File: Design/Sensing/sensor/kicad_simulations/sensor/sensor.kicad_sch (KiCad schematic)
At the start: 44 parts, among them J1 Conn_02x14_Counter_Clockwise, J10 Conn_01x02_Pin, J11 Conn_01x01_Pin, J12 Conn_01x02_Pin, J13 Conn_01x02_Pin, J14 Conn_01x02_Pin, J15 Conn_01x02_Pin, J16 Conn_01x01_Pin, J17 Conn_01x02_Pin, J18 Conn_01x01_Pin, J3 Conn_01x02_Pin, J4 Conn_01x02_Pin, J5 Conn_01x02_Pin, J6 Conn_01x01_Pin, J7 Conn_01x02_Pin, J8 Conn_01x02_Pin, J9 Conn_01x02_Pin, Q1 2N3904, Q2 2N3904, Q3 2N3904, U1 TSSP58038, U2 TSSP58038, U3 TSSP58038, U4 BUF602xD, U5 BUF602xD, U6 BUF602xD

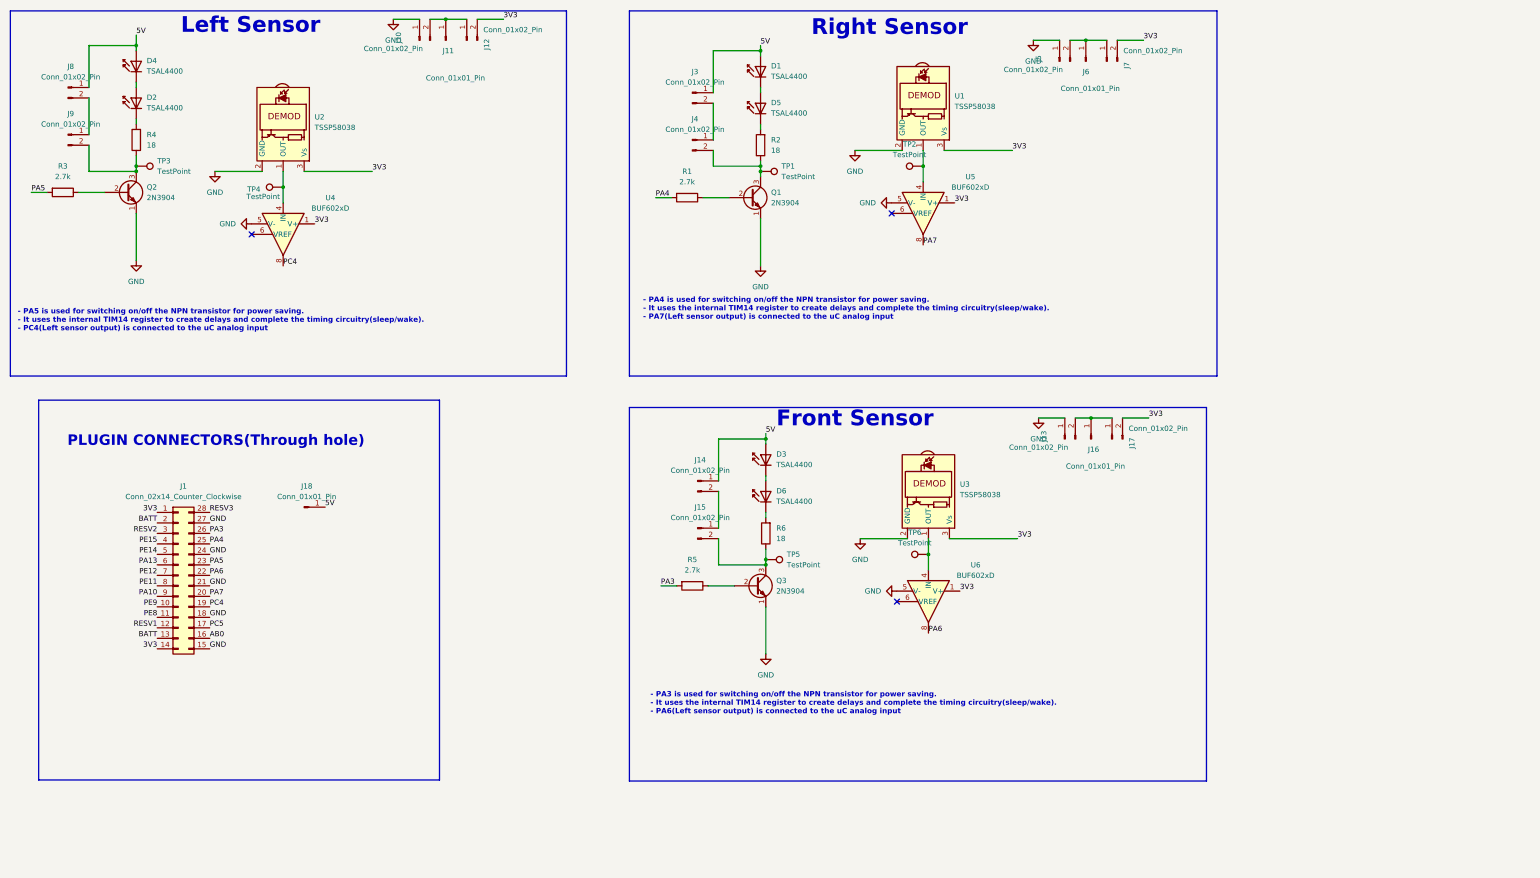
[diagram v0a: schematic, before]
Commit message: PCB placement done, now need to root/make track connections
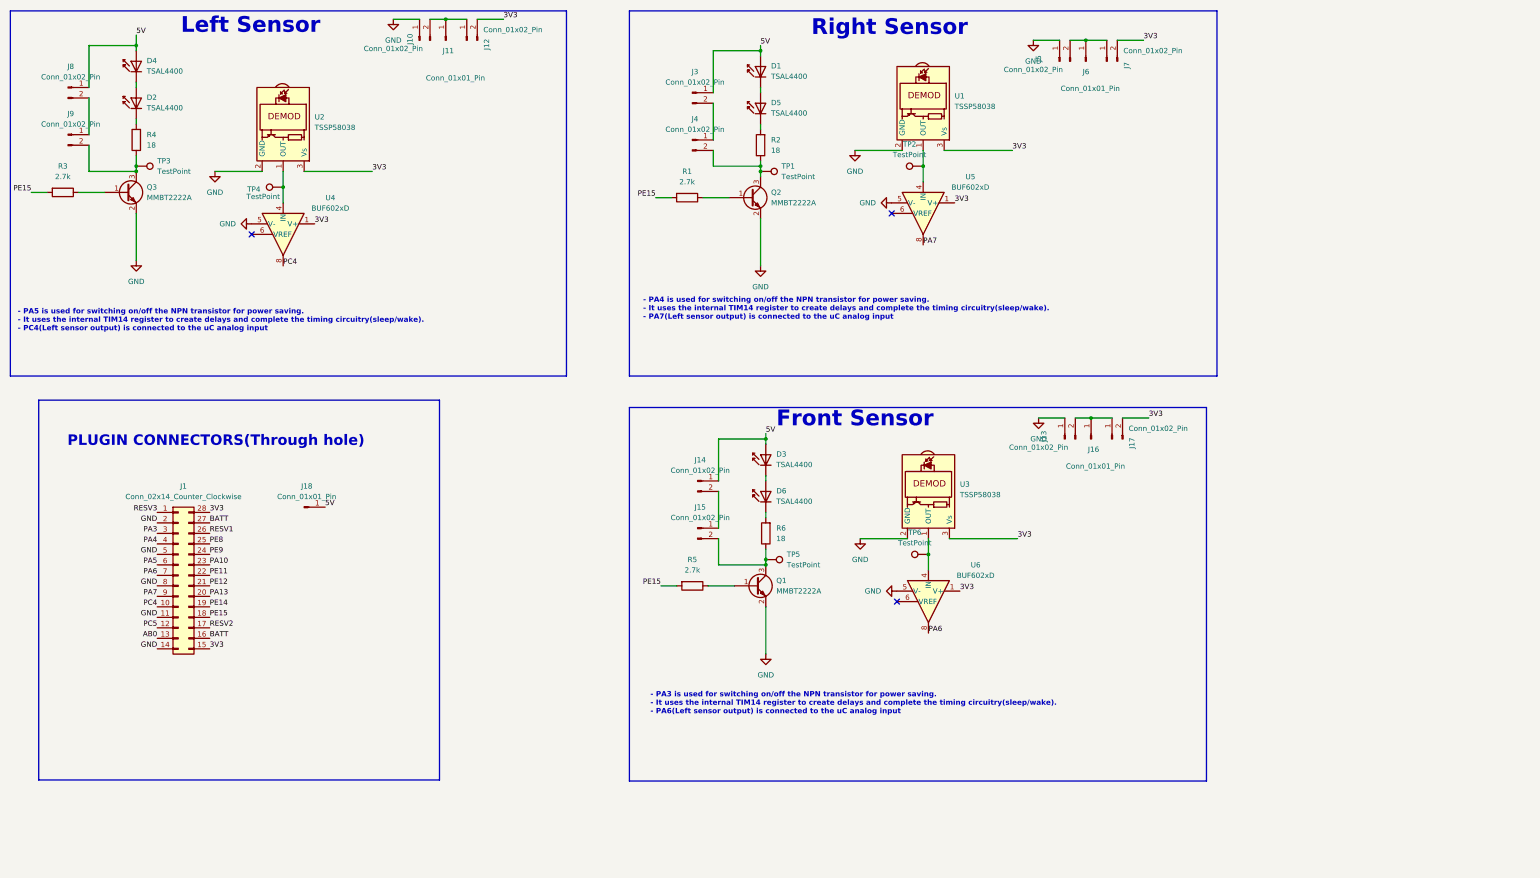
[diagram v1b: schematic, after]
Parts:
- removed Q1, Q2, Q3: 2N3904, Package_TO_SOT_THT:TO-92_Inline, symbol Transistor_BJT:2N3904
- added Q1, Q2, Q3: MMBT2222A, Package_TO_SOT_SMD:SOT-23, symbol Transistor_BJT:MMBT2222A
- D1, D2, D3, D4, D5, D6: footprint LED_THT:LED_D3.0mm_IRBlack -> LED_THT:LED_D3.0mm_Horizontal_O1.27mm_Z2.0mm_IRBlack
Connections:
- net 3V3: now also J1.15 (Pin_15), J1.28 (Pin_28); no longer J1.1 (Pin_1), J1.14 (Pin_14)
- net AB0: now also J1.13 (Pin_13); no longer J1.16 (Pin_16)
- net BATT: now also J1.16 (Pin_16), J1.27 (Pin_27); no longer J1.13 (Pin_13), J1.2 (Pin_2)
- net GND: now also J1.11 (Pin_11), J1.14 (Pin_14), J1.2 (Pin_2), J1.5 (Pin_5), J1.8 (Pin_8), Q1.2 (E), Q2.2 (E), Q3.2 (E); no longer J1.15 (Pin_15), J1.18 (Pin_18), J1.21 (Pin_21), J1.24 (Pin_24), J1.27 (Pin_27)
- net PA10: now also J1.23 (Pin_23); no longer J1.9 (Pin_9)
- net PA13: now also J1.20 (Pin_20); no longer J1.6 (Pin_6)
- net PA3: now also J1.3 (Pin_3); no longer J1.26 (Pin_26), R5.2
- net PA4: now also J1.4 (Pin_4); no longer J1.25 (Pin_25), R1.2
- net PA5: now also J1.6 (Pin_6); no longer J1.23 (Pin_23), R3.2
- net PA6: now also J1.7 (Pin_7); no longer J1.22 (Pin_22)
- net PA7: now also J1.9 (Pin_9); no longer J1.20 (Pin_20)
- net PC4: now also J1.10 (Pin_10); no longer J1.19 (Pin_19)
- net PC5: now also J1.12 (Pin_12); no longer J1.17 (Pin_17)
- net PE11: now also J1.22 (Pin_22); no longer J1.8 (Pin_8)
- net PE12: now also J1.21 (Pin_21); no longer J1.7 (Pin_7)
- net PE14: now also J1.19 (Pin_19); no longer J1.5 (Pin_5)
- net PE15: now also J1.18 (Pin_18), R1.2, R3.2, R5.2; no longer J1.4 (Pin_4)
- net PE8: now also J1.25 (Pin_25); no longer J1.11 (Pin_11)
- net PE9: now also J1.24 (Pin_24); no longer J1.10 (Pin_10)
- net RESV1: now also J1.26 (Pin_26); no longer J1.12 (Pin_12)
- net RESV2: now also J1.17 (Pin_17); no longer J1.3 (Pin_3)
- net RESV3: now also J1.1 (Pin_1); no longer J1.28 (Pin_28)
- net at R5.1: now also Q1.1 (B)
- net at J15.2 (Pin_2), R6.1, TP5.1: now also Q1.3 (C)
- net at J9.2 (Pin_2), R4.1, TP3.1: now also Q3.3 (C)
- net at R1.1: now also Q2.1 (B)
- net at J4.2 (Pin_2), R2.1, TP1.1: now also Q2.3 (C)
- net at R3.1: now also Q3.1 (B)

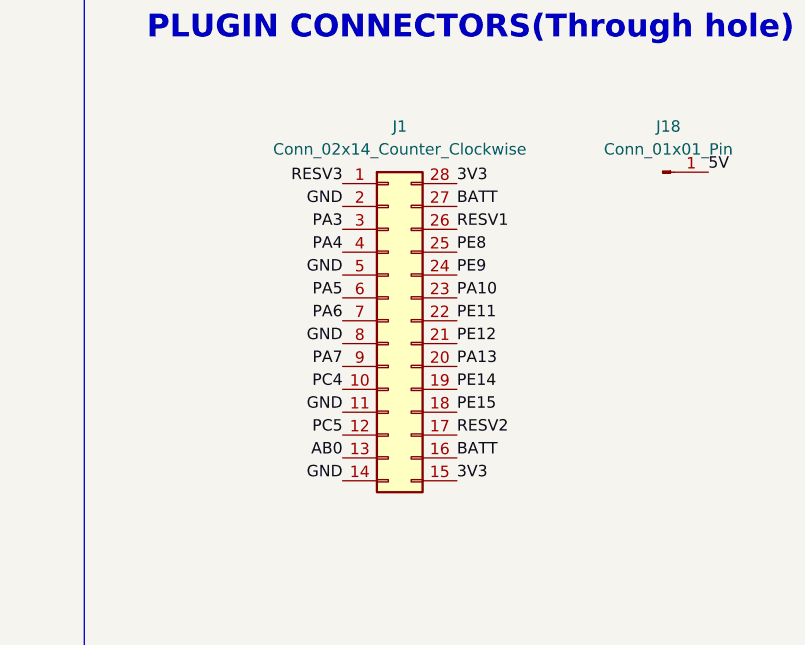
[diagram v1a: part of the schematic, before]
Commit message: PCB track done but still have 23 unrouted
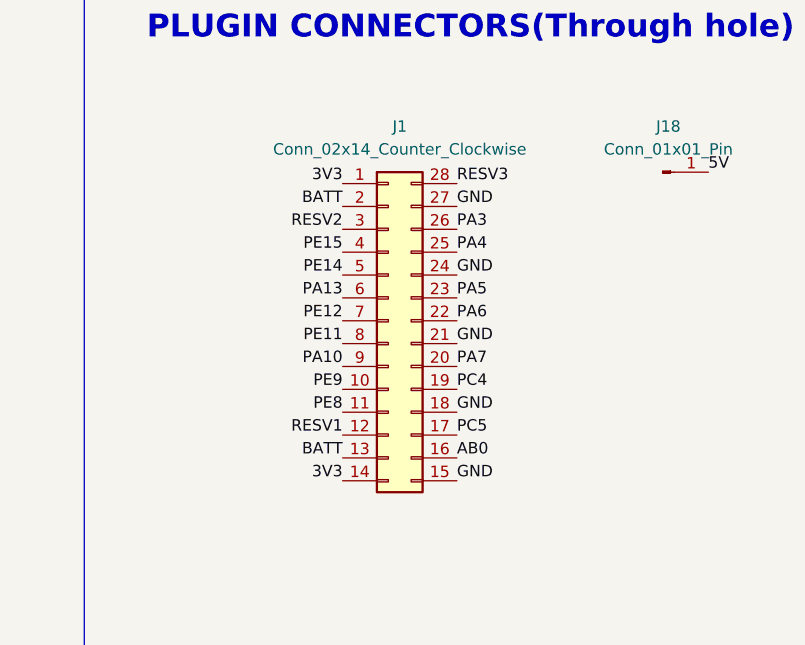
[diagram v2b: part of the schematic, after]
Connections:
- net 3V3: now also J1.1 (Pin_1), J1.14 (Pin_14); no longer J1.15 (Pin_15), J1.28 (Pin_28)
- net AB0: now also J1.16 (Pin_16); no longer J1.13 (Pin_13)
- net BATT: now also J1.13 (Pin_13), J1.2 (Pin_2); no longer J1.16 (Pin_16), J1.27 (Pin_27)
- net GND: now also J1.15 (Pin_15), J1.18 (Pin_18), J1.21 (Pin_21), J1.24 (Pin_24), J1.27 (Pin_27); no longer J1.11 (Pin_11), J1.14 (Pin_14), J1.2 (Pin_2), J1.5 (Pin_5), J1.8 (Pin_8)
- net PA10: now also J1.9 (Pin_9); no longer J1.23 (Pin_23)
- net PA13: now also J1.6 (Pin_6); no longer J1.20 (Pin_20)
- net PA3: now also J1.26 (Pin_26); no longer J1.3 (Pin_3)
- net PA4: now also J1.25 (Pin_25); no longer J1.4 (Pin_4)
- net PA5: now also J1.23 (Pin_23); no longer J1.6 (Pin_6)
- net PA6: now also J1.22 (Pin_22); no longer J1.7 (Pin_7)
- net PA7: now also J1.20 (Pin_20); no longer J1.9 (Pin_9)
- net PC4: now also J1.19 (Pin_19); no longer J1.10 (Pin_10)
- net PC5: now also J1.17 (Pin_17); no longer J1.12 (Pin_12)
- net PE11: now also J1.8 (Pin_8); no longer J1.22 (Pin_22)
- net PE12: now also J1.7 (Pin_7); no longer J1.21 (Pin_21)
- net PE14: now also J1.5 (Pin_5); no longer J1.19 (Pin_19)
- net PE15: now also J1.4 (Pin_4); no longer J1.18 (Pin_18)
- net PE8: now also J1.11 (Pin_11); no longer J1.25 (Pin_25)
- net PE9: now also J1.10 (Pin_10); no longer J1.24 (Pin_24)
- net RESV1: now also J1.12 (Pin_12); no longer J1.26 (Pin_26)
- net RESV2: now also J1.3 (Pin_3); no longer J1.17 (Pin_17)
- net RESV3: now also J1.28 (Pin_28); no longer J1.1 (Pin_1)

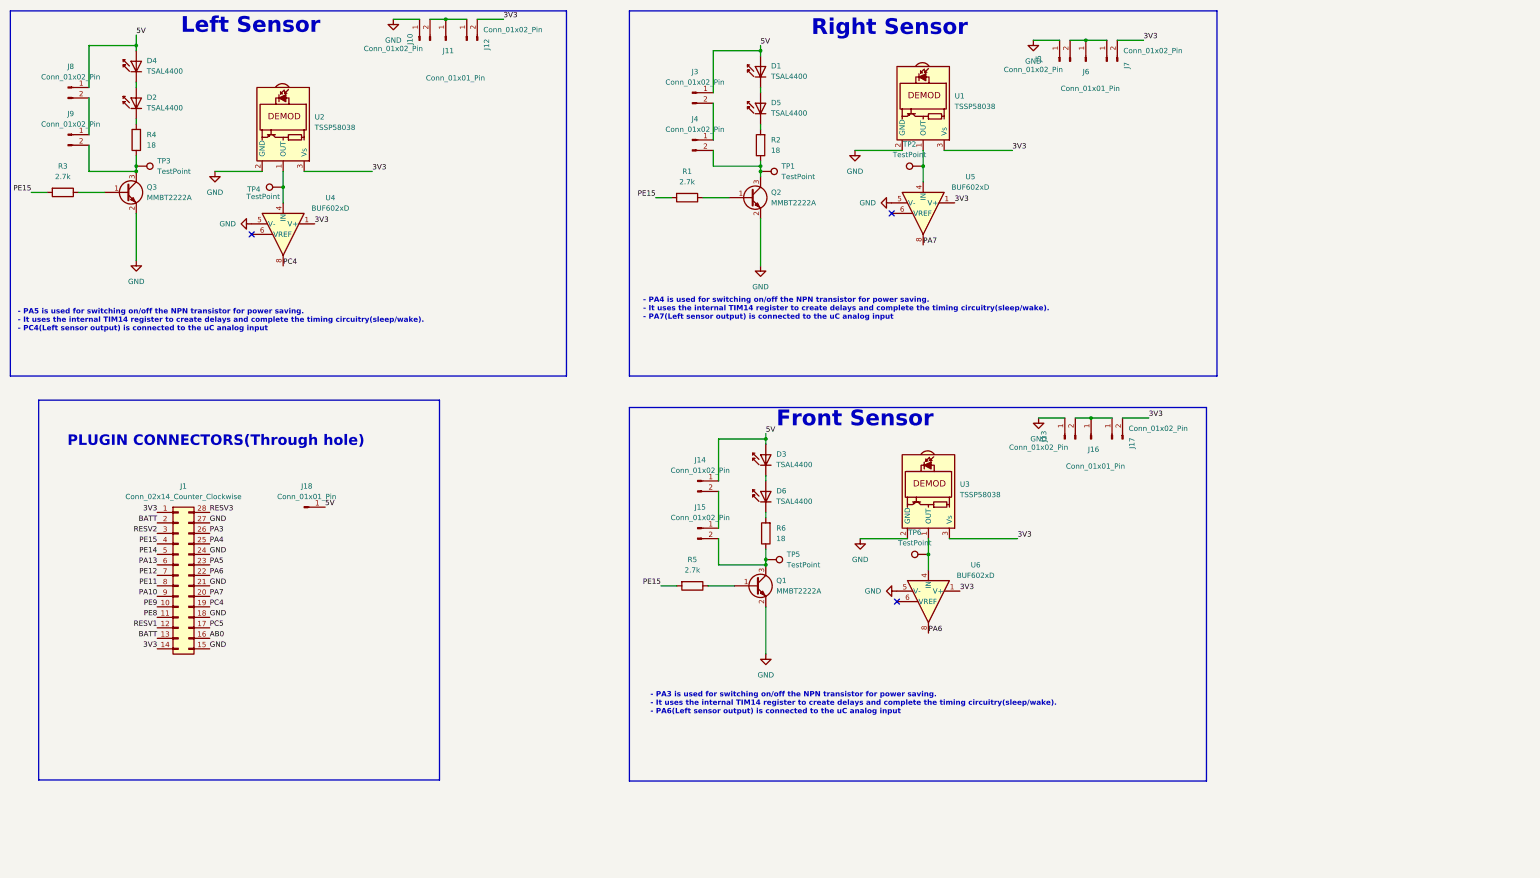
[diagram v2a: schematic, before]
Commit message: Only two unrouted and 3 errors remaining
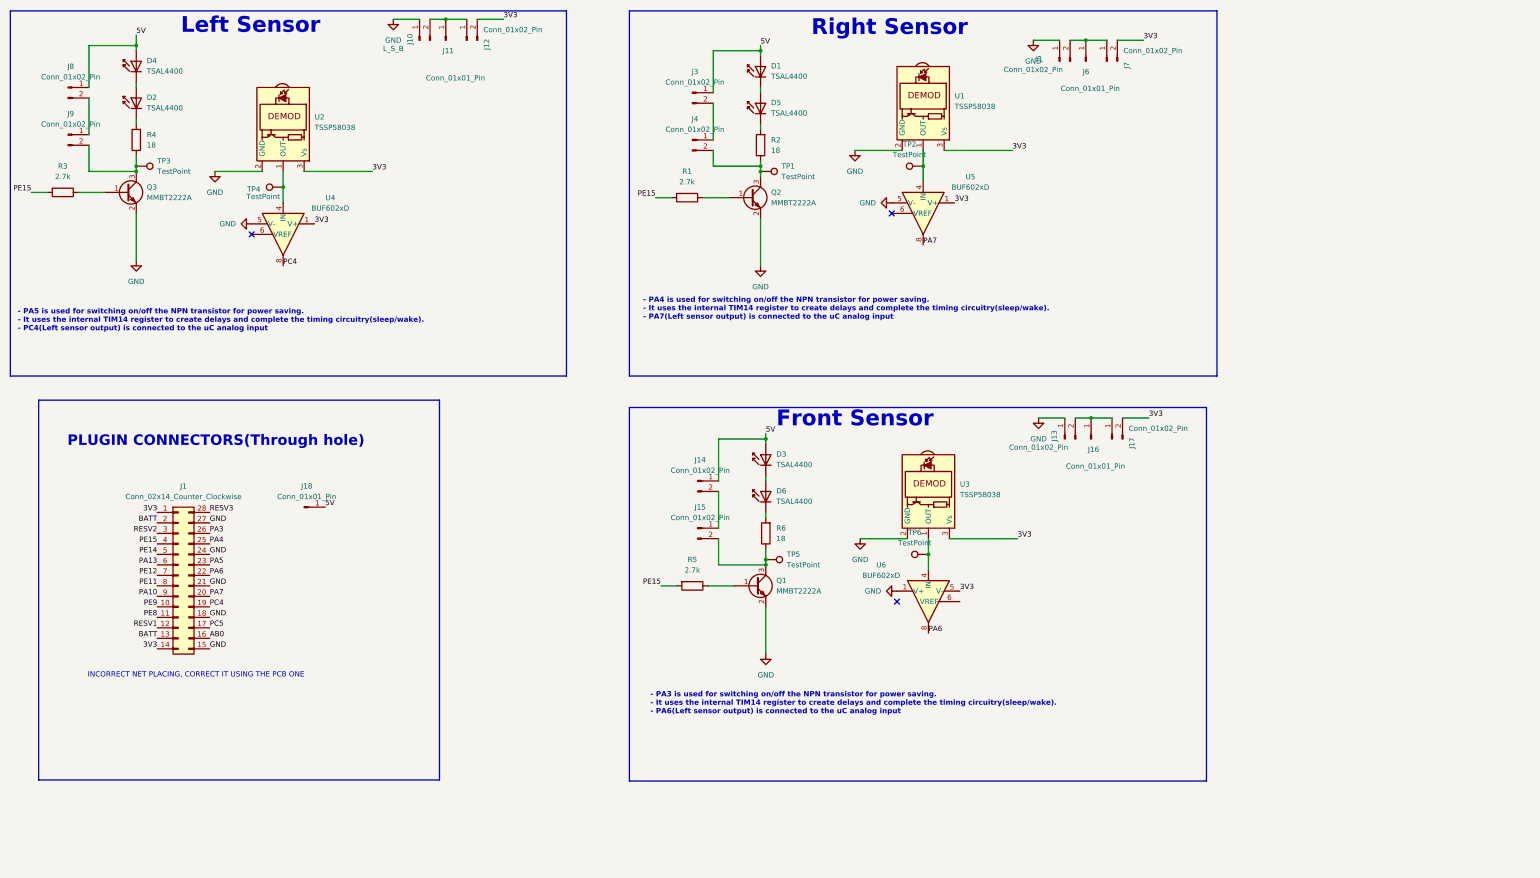
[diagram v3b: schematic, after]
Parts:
- J10: value Conn_01x02_Pin -> L_S_B
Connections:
- net 3V3: now also U6.5 (V-); no longer U6.1 (V+)
- net GND: now also U6.1 (V+); no longer U6.5 (V-)
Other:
- note added: "INCORRECT NET PLACING, CORRECT IT USING THE PCB ONE"
- moved on the sheet: U6
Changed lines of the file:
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@@
 		)
 	)
+	(text "INCORRECT NET PLACING, CORRECT IT USING THE PCB ONE\n"
+		(exclude_from_sim no)
+		(at 75.438 181.61 0)
+		(effects
+			(font
+				(size 1.27 1.27)
+			)
+		)
+	)
 	(text "- PA4 is used for switching on/off the NPN transistor for power saving.\n- It uses the internal TIM14 register to create delays and complete the timing circuitry(sleep/wake).\n- PA7(Left sensor output) is connected to the uC analog input"
 		(exclude_from_sim no)
@@
 			)
 		)
-		(property "Value" "Conn_01x02_Pin"
+		(property "Value" "L_S_B"
 			(at 123.19 29.972 90)
 			(effects
@@
 		(dnp no)
 		(property "Reference" "J13"
-			(at 280.67 123.825 0)
+			(at 283.21 123.698 0)
 			(effects
 				(font
@@
 		(on_board yes)
 		(dnp no)
-		(fields_autoplaced yes)
 		(property "Reference" "Q2"
 			(at 214.63 64.7699 0)
@@
 	(symbol
 		(lib_id "Amplifier_Buffer:BUF602xD")
-		(at 252.73 163.83 270)
+		(at 252.73 163.83 90)
+		(mirror x)
 		(unit 1)
 		(exclude_from_sim no)
@@
 		(on_board yes)
 		(dnp no)
-		(fields_autoplaced yes)
 		(property "Reference" "U6"
-			(at 264.16 154.9714 90)
+			(at 241.3 154.9714 90)
 			(effects
 				(font
@@
 		)
 		(property "Value" "BUF602xD"
-			(at 264.16 157.5114 90)
+			(at 241.3 157.5114 90)
 			(effects
 				(font
@@
 		)
 		(property "Footprint" "Package_SO:SOIC-8_3.9x4.9mm_P1.27mm"
-			(at 245.11 163.83 0)
+			(at 260.35 163.83 0)
 			(effects
 				(font

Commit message: pcb placement redo
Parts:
- removed J1: Conn_02x14_Counter_Clockwise, Connector_PinSocket_2.54mm:PinSocket_2x14_P2.54mm_Vertical, symbol Connector_Generic:Conn_02x14_Counter_Clockwise
- removed J11, J16, J18: Conn_01x01_Pin, Connector_PinHeader_2.54mm:PinHeader_1x01_P2.54mm_Vertical, symbol Connector:Conn_01x01_Pin
- removed J14, J15, J3, J4: Conn_01x02_Pin, Connector_PinHeader_2.54mm:PinHeader_1x02_P2.54mm_Vertical, symbol Connector:Conn_01x02_Pin
- removed Q1, Q2, Q3: MMBT2222A, Package_TO_SOT_SMD:SOT-23, symbol Transistor_BJT:MMBT2222A
- removed U1: TSSP58038, OptoDevice:Vishay_MINICAST-3Pin, symbol Sensor_Proximity:TSSP58038
- removed U4, U5, U6: BUF602xD, Package_SO:SOIC-8_3.9x4.9mm_P1.27mm, symbol Amplifier_Buffer:BUF602xD
- added J1, J11, J16, J2: Conn_01x02_Pin, Connector_PinHeader_2.54mm:PinHeader_1x02_P2.54mm_Vertical, symbol Connector:Conn_01x02_Pin
- added J14, J15, J4: Conn_01x01_Pin, Connector_PinHeader_2.54mm:PinHeader_1x01_P2.54mm_Vertical, symbol Connector:Conn_01x01_Pin
- added J3: Conn_02x14_Counter_Clockwise, Connector_PinSocket_2.54mm:PinSocket_2x14_P2.54mm_Vertical, symbol Connector_Generic:Conn_02x14_Counter_Clockwise
- added Q1, Q2, Q3: MMBT5551L, Package_TO_SOT_SMD:SOT-23, symbol Transistor_BJT:MMBT5551L
- added U1: LM324, Package_SO:SOIC-14_3.9x8.7mm_P1.27mm, symbol Amplifier_Operational:LM324
- added U4: TSSP58038, OptoDevice:Vishay_MINICAST-3Pin, symbol Sensor_Proximity:TSSP58038
- J10: value L_S_B -> Conn_01x02_Pin
- J5: value Conn_01x02_Pin -> L_S_B
- R4: value 18 -> 2.7k
- R5: value 2.7k -> 18
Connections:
- net 3V3: now also J16.2 (Pin_2), J3.1 (Pin_1), J3.14 (Pin_14), U1.4 (V+), U4.3 (Vs); no longer J12.2 (Pin_2)
- net 5V: now also D5.2 (A), J10.1 (Pin_1), J1.1 (Pin_1), J4.1 (Pin_1); no longer D4.2 (A)
- net AB0: now also J3.16 (Pin_16)
- net BATT: now also J3.13 (Pin_13), J3.2 (Pin_2)
- net GND: now also J12.1 (Pin_1), J3.15 (Pin_15), J3.18 (Pin_18), J3.21 (Pin_21), J3.24 (Pin_24), J3.27 (Pin_27), Q1.2 (E), Q2.2 (E), Q3.2 (E), U1.11 (V-), U4.2 (GND); no longer J10.1 (Pin_1)
- net PA10: now also J3.9 (Pin_9)
- net PA13: now also J3.6 (Pin_6)
- net PA3: now also J3.26 (Pin_26)
- net PA4: now also J3.25 (Pin_25)
- net PA5: now also J3.23 (Pin_23)
- net PA6: now also J3.22 (Pin_22), U1.8, U1.9 (-)
- net PA7: now also J3.20 (Pin_20), U1.6 (-), U1.7
- net PC4: now also J3.19 (Pin_19), U1.1, U1.2 (-)
- net PC5: now also J3.17 (Pin_17)
- net PE11: now also J3.8 (Pin_8)
- net PE12: now also J3.7 (Pin_7)
- net PE14: now also J3.5 (Pin_5)
- net PE15: now also R4.2, J3.4 (Pin_4); no longer R5.2
- net PE8: now also J3.11 (Pin_11)
- net PE9: now also J3.10 (Pin_10)
- net RESV1: now also J3.12 (Pin_12)
- net RESV2: now also J3.3 (Pin_3)
- net RESV3: now also J3.28 (Pin_28)
- net at J10.2 (Pin_2): now also J11.1 (Pin_1); no longer J12.1 (Pin_1)
- net at D4.1 (K): now also R5.2; no longer D2.2 (A)
- net at U3.1 (OUT): now also TP5.1, U1.5 (+); no longer TP6.1
- net at TP4.1: now also R6.1, J11.2 (Pin_2), Q3.3 (C); no longer U2.1 (OUT)
- net at D2.1 (K): now also R2.2; no longer R4.2
- net at J9.2 (Pin_2), TP3.1: now also R5.1, Q2.3 (C); no longer R4.1
- net at D3.1 (K): now also D4.2 (A); no longer D6.2 (A)
- net at D5.1 (K): now also D6.2 (A); no longer R2.2
- net at D1.1 (K): now also D2.2 (A); no longer D5.2 (A)
- net at R3.1: now also Q2.1 (B)
- net at J13.2 (Pin_2), J17.1 (Pin_1): now also J15.1 (Pin_1)
- net at R1.1: now also Q1.1 (B)
- net at TP2.1: now also U2.1 (OUT), U1.3 (+)
- net at R2.1, TP1.1: now also J2.2 (Pin_2), Q1.3 (C)
- new net: J12.2 (Pin_2), J14.1 (Pin_1), J16.1 (Pin_1)
- new net: Q3.1 (B), R4.1
- new net: TP6.1, U1.10 (+), U4.1 (OUT)
- new net: J1.2 (Pin_2), J2.1 (Pin_1)
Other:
- note added: "Op Amp power rails"
